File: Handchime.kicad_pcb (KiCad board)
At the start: 2 copper layers, 40.6 x 16.5 mm, 24 parts, among them J1 USB_C_Receptacle_USB2.0_16P, J2 Pins, J3 SWD, SW0 BOOT, SW1 Row 0, Col 0, SW2 Row 0, Col 1, U1 STM32C071GBUx, U2 PRTR5V0U2X, U3 XC6206P332MR-G

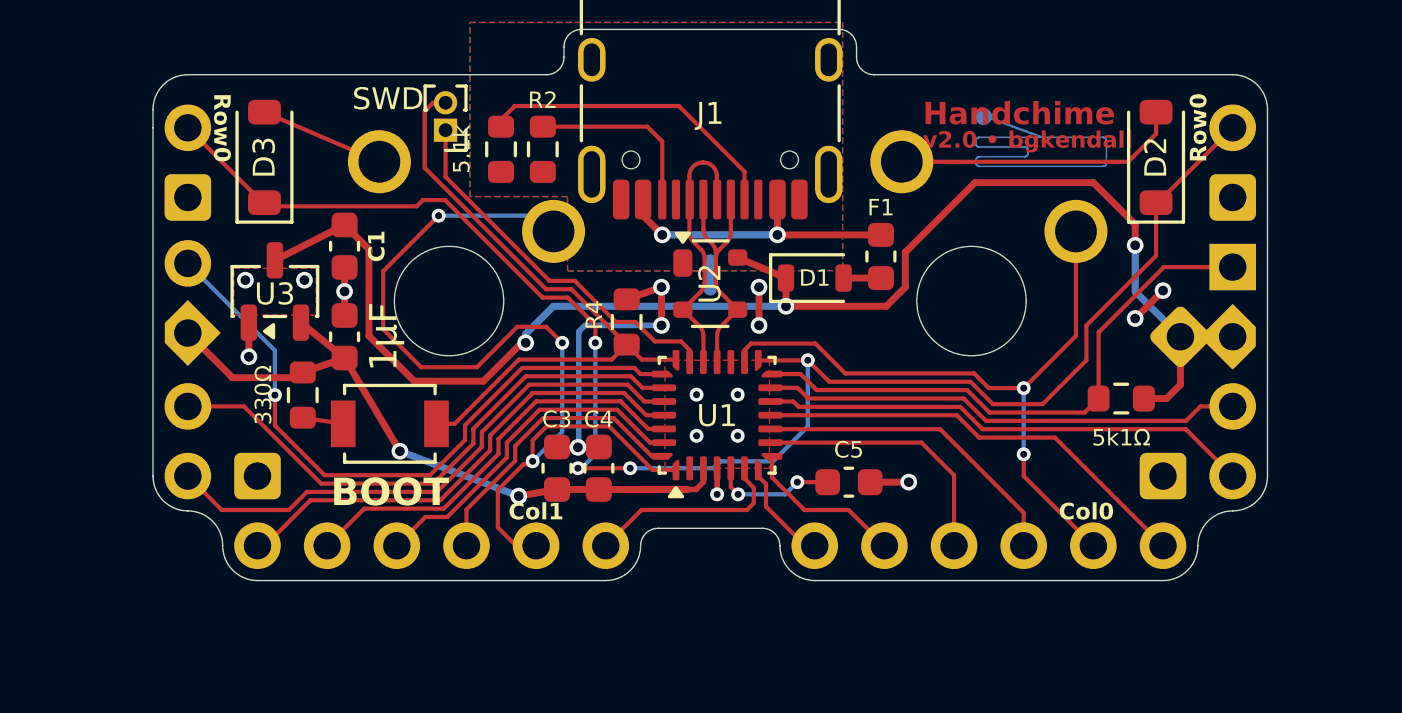
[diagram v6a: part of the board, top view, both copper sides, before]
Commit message: Fix edge pin alignment and improve silkscreen
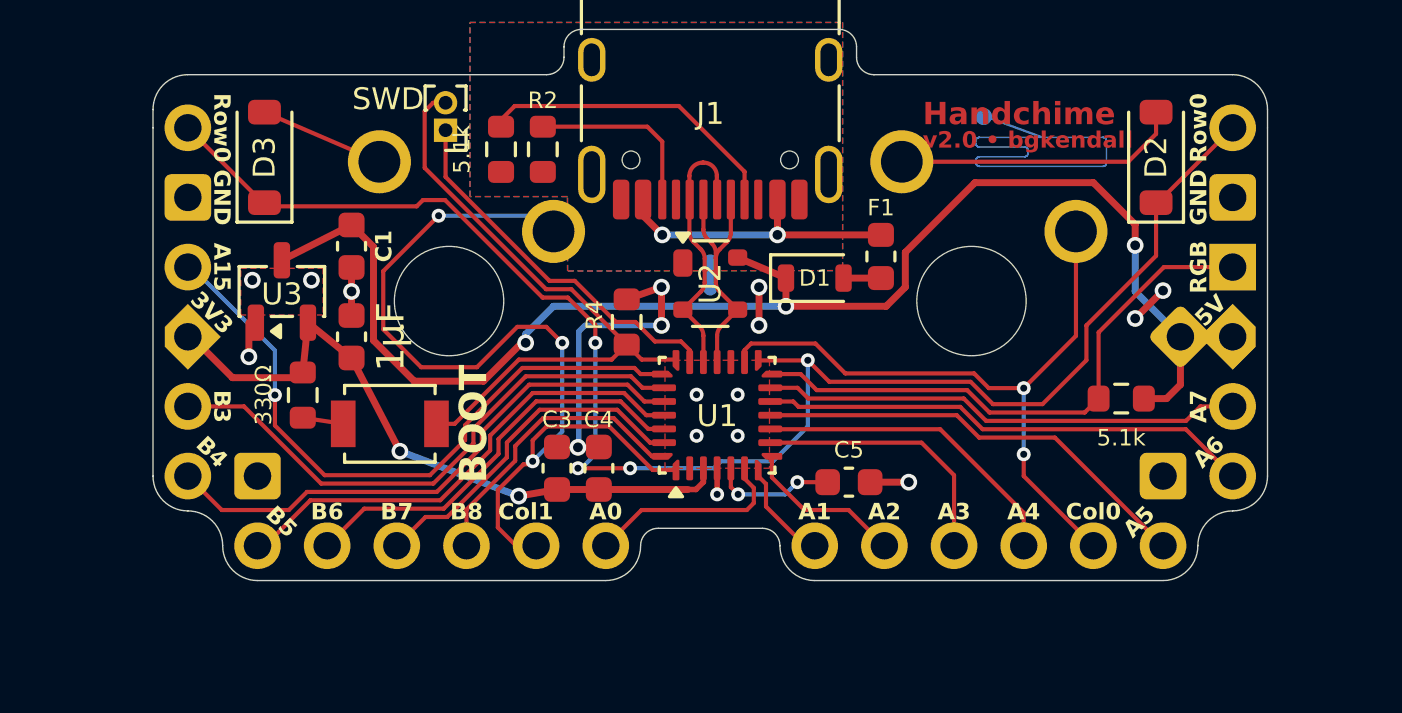
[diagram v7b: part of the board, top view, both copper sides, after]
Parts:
- R3: value 5k1Ω -> 5.1k
- moved C1 0.25 mm to (139.3, 48.8)
- moved C2 0.25 mm to (139.3, 52.1)
- moved U3 0.25 mm to (136.8, 50.5)

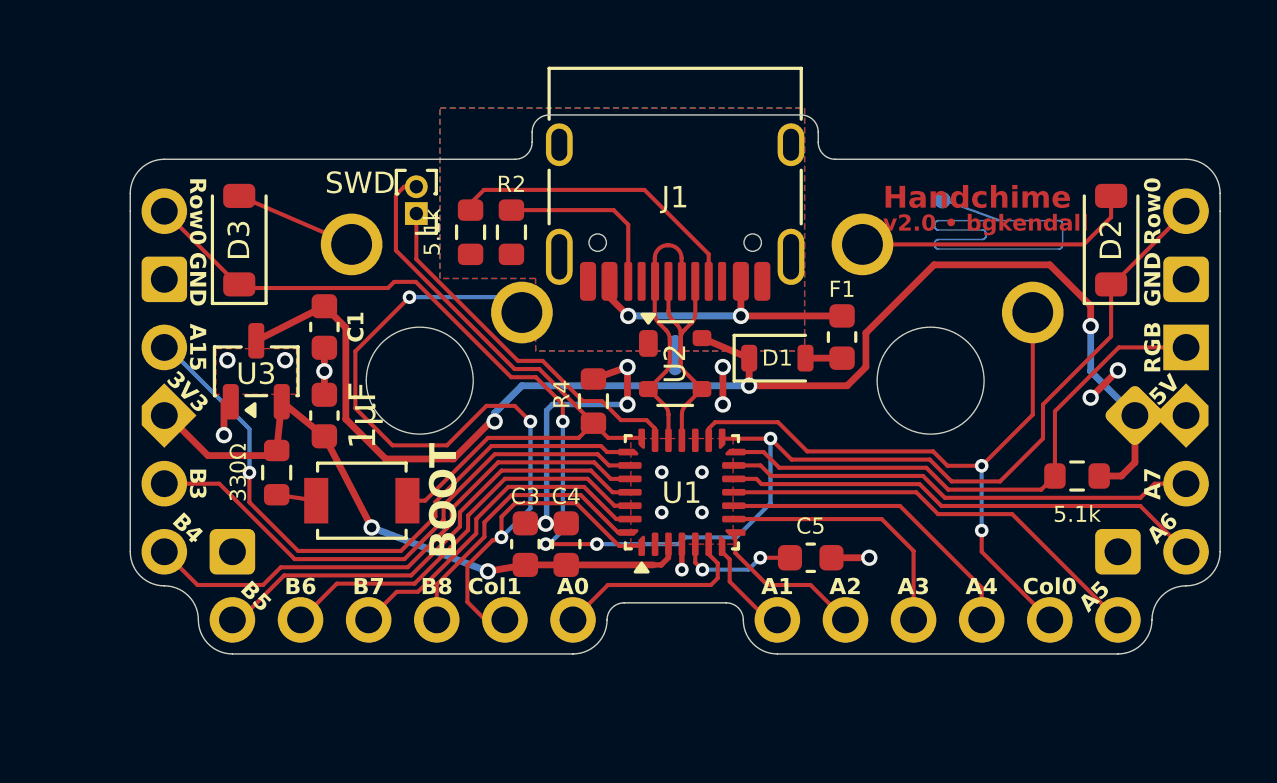
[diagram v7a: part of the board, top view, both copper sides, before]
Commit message: Use values instead of references for resistor and capacitor silkscreens
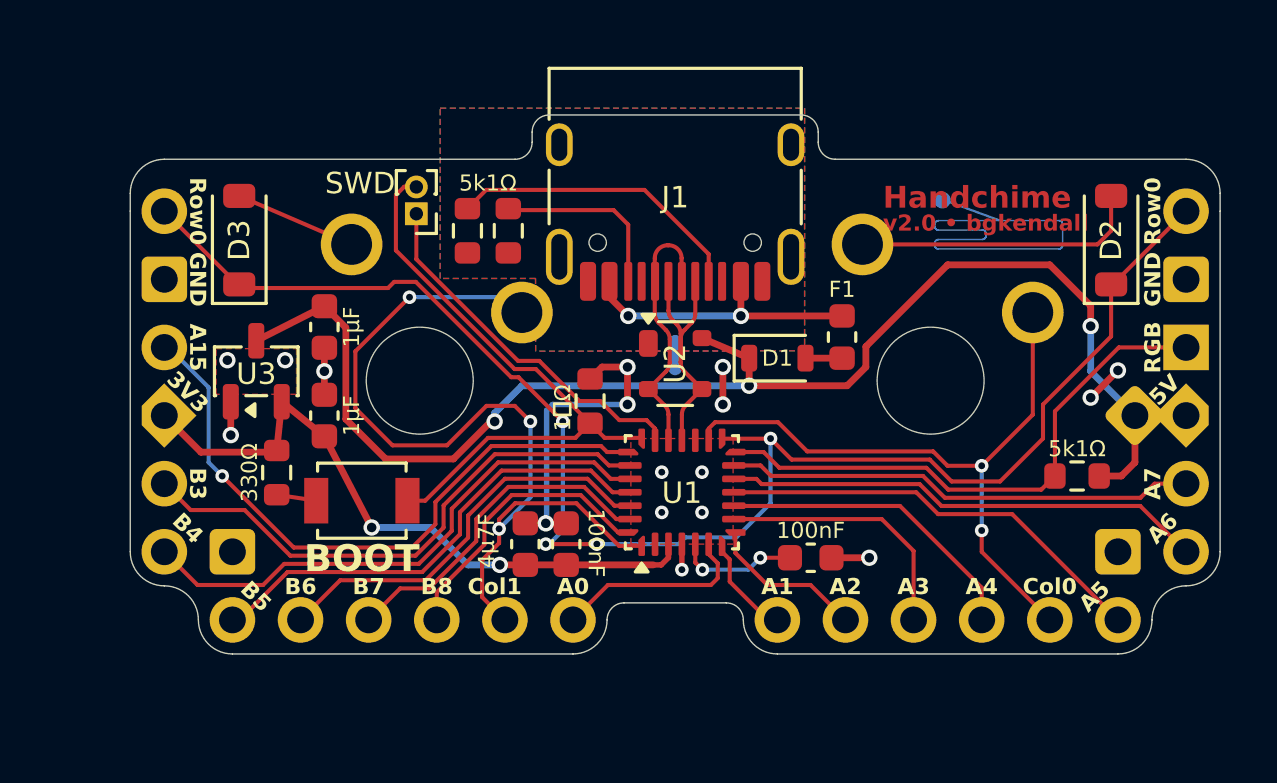
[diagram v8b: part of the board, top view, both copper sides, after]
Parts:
- C3: value 4.7µF -> 4µ7F
- R1, R2, R3: value 5.1k -> 5k1Ω
- moved R1 0.13 mm to (144.7, 45.2)
- moved R2 0.13 mm to (146.2, 45.2)
- moved R4 0.13 mm to (149.2, 51.6)
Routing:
- net C1: track 33.7 -> 32.4 mm
